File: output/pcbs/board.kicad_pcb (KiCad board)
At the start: 2 copper layers, 94 x 86 mm, 38 parts

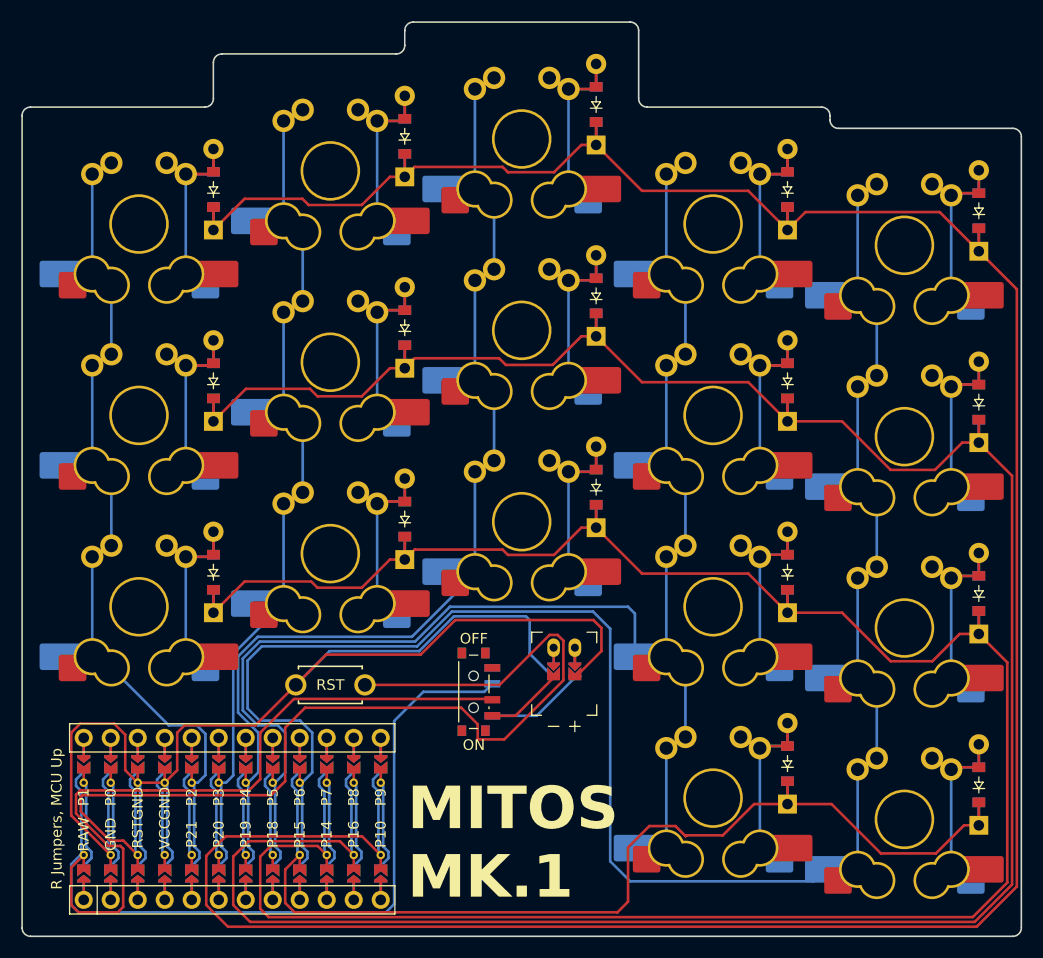
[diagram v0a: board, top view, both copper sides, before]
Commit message: update file sturecture, add jlcnumber
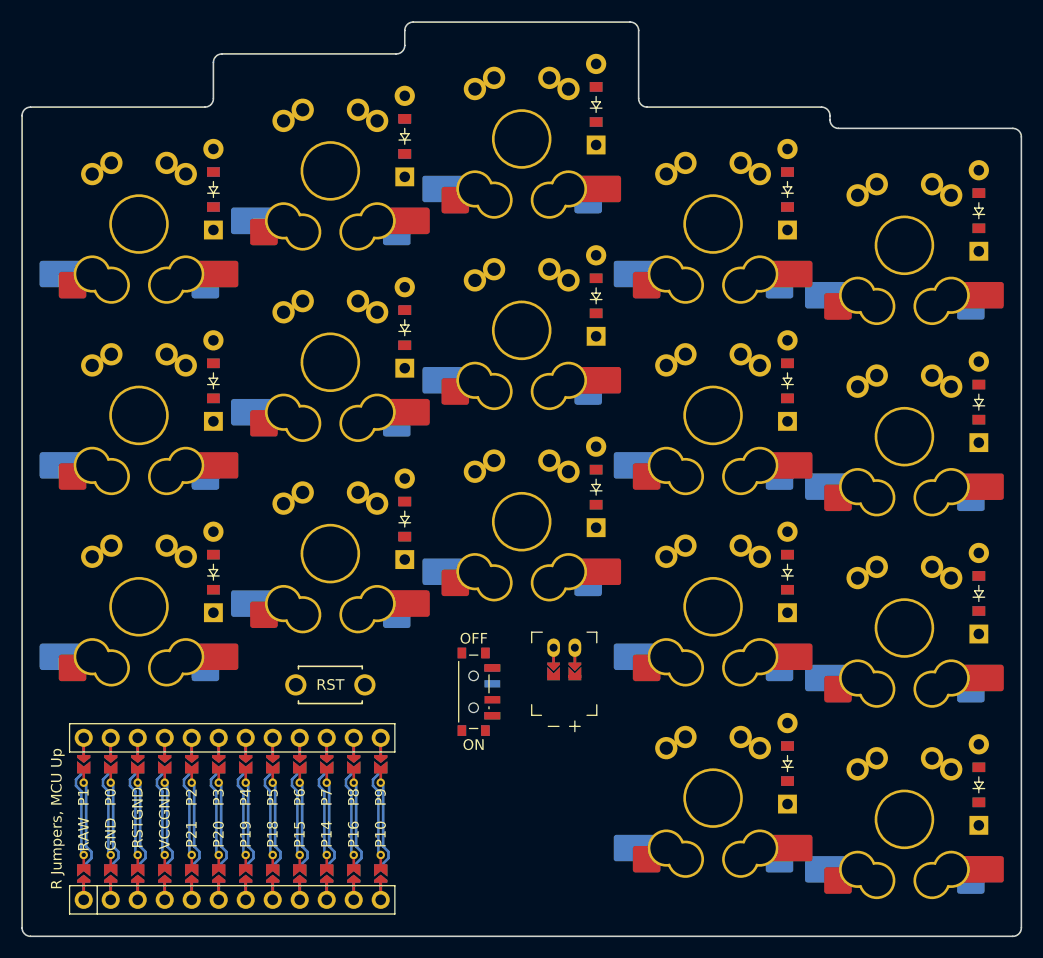
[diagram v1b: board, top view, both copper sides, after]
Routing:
- net (no net): track 0.00 -> 337.7 mm
- net P10: track 275.6 -> 0.00 mm
- net P16: track 249.4 -> 0.00 mm
- net P14: track 222.3 -> 0.00 mm
- net P6: track 163.9 -> 0.00 mm
- net RAW: track 143.2 -> 0.00 mm
- net GND: track 142.6 -> 0.00 mm
- net P5: track 125.2 -> 0.00 mm
- net P15: track 100.2 -> 0.00 mm
- net RST: track 99.3 -> 0.00 mm
- net P4: track 91.2 -> 0.00 mm
- net P3: track 70.8 -> 0.00 mm
- net P2: track 67.9 -> 0.00 mm
- net index_bottom: track 20.9 -> 0.00 mm
- net middle_bottom: track 19.6 -> 0.00 mm
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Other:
- net class Default added: clearance 0.2, trace_width 0.25, via_dia 0.8, via_drill 0.4
- board text removed: "MITOS B.JH"
- board text removed: "MITOS MK.1"
